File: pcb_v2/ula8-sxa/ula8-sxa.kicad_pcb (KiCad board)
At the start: 2 copper layers, 54.4 x 61 mm, 7 parts, among them J1 ula8a, U1 74LS244

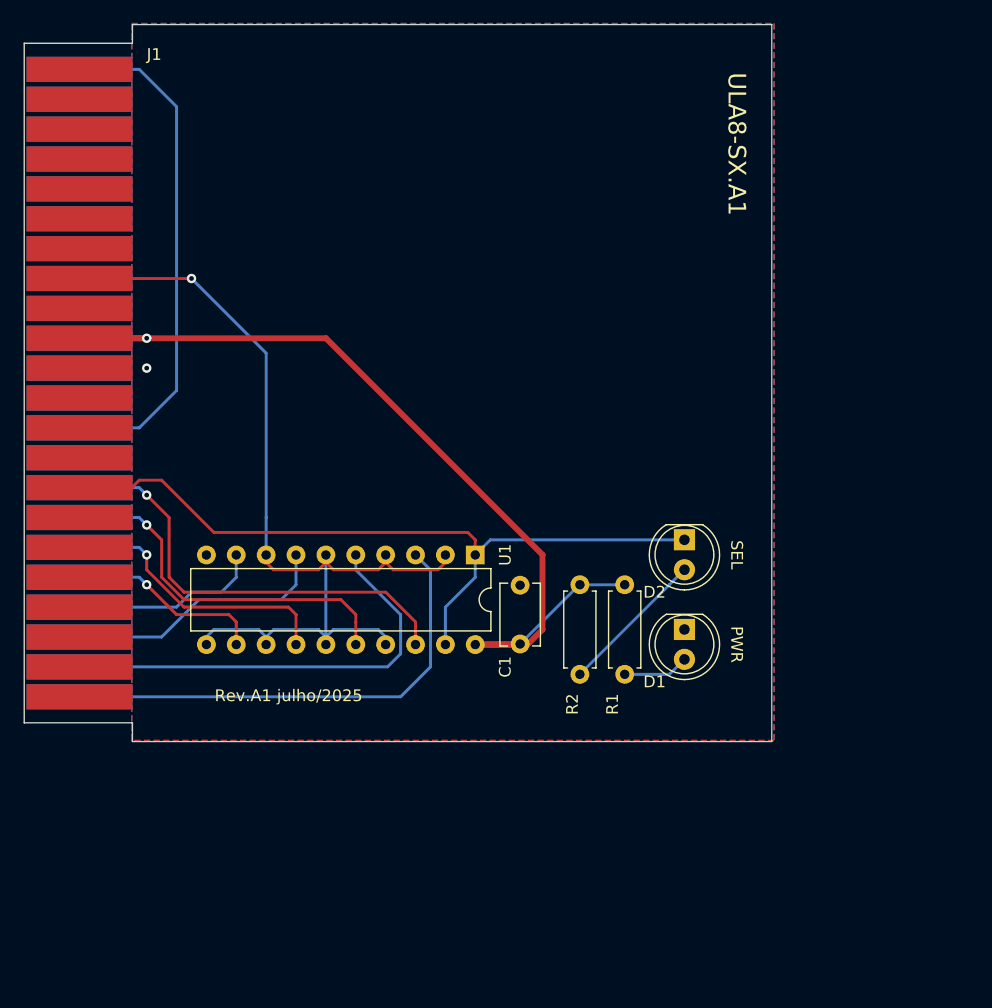
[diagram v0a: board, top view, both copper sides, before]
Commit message: deslocando alimentação para as estremidades do conector; carry out em três estados (ativo apenas quando select)
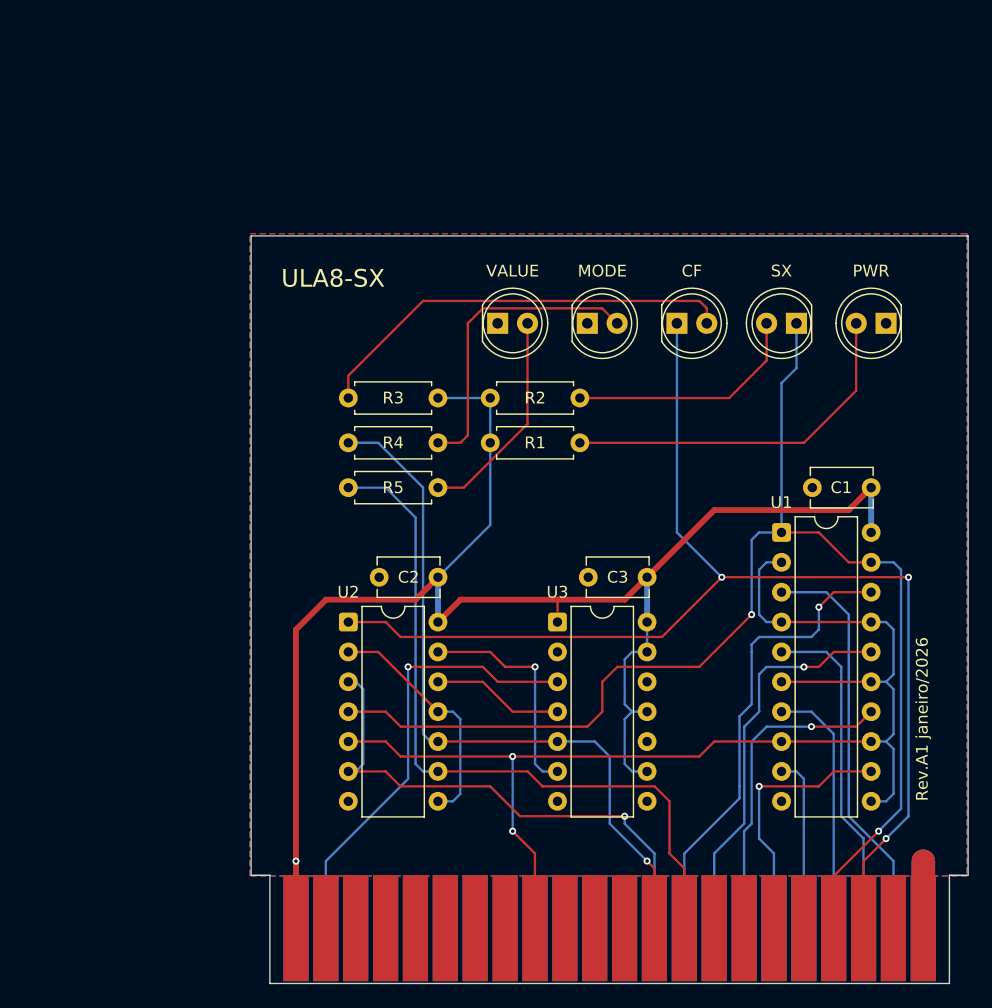
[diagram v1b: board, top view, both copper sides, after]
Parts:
- added C2: 100nF, Capacitor_THT:C_Disc_D5.1mm_W3.2mm_P5.00mm, F.Cu at (42.0, 57.1)
- added C3: 100nF, Capacitor_THT:C_Disc_D5.1mm_W3.2mm_P5.00mm, F.Cu at (59.8, 57.1)
- added D3: LED, LED_THT:LED_D5.0mm, F.Cu at (67.3, 35.6)
- added D4: LED, LED_THT:LED_D5.0mm, F.Cu at (59.7, 35.6)
- added D5: LED, LED_THT:LED_D5.0mm, F.Cu at (52.1, 35.6)
- added R3: 1K, Resistor_THT:R_Axial_DIN0207_L6.3mm_D2.5mm_P7.62mm_Horizontal, F.Cu at (47.0, 41.9)
- added R4: 1K, Resistor_THT:R_Axial_DIN0207_L6.3mm_D2.5mm_P7.62mm_Horizontal, F.Cu at (39.4, 45.7)
- added R5: 1K, Resistor_THT:R_Axial_DIN0207_L6.3mm_D2.5mm_P7.62mm_Horizontal, F.Cu at (39.4, 49.5)
- added U2: 74LS125, Package_DIP:DIP-14_W7.62mm, F.Cu at (39.4, 61.0)
- added U3: 74LS04, Package_DIP:DIP-14_W7.62mm, F.Cu at (57.1, 61.0)
- moved J1 75.3 mm to (34.9, 87.0), turned to 90 degrees
- moved D1 31.2 mm to (85.1, 35.6), turned to 180 degrees
- moved C1 26.2 mm to (78.8, 49.5), turned to 0 degrees
- moved U1 26.1 mm to (76.2, 53.3), turned to 0 degrees
- moved D2 20.7 mm to (77.5, 35.6), turned to 180 degrees
- moved R2 17.6 mm to (51.4, 41.9), turned to 0 degrees
- moved R1 16.6 mm to (51.4, 45.7), turned to 0 degrees
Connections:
- D2 pad 1: n_select -> ~{select_sx}
- J1 pad 1: unconnected-(J1-Pad1) -> +5V
- J1 pad 10: +5V -> unconnected-(J1-Pin_10-Pad10)
- J1 pad 11: GND -> unconnected-(J1-Pin_11-Pad11)
- J1 pad 13: unconnected-(J1-Pad13) -> option_mode
- J1 pad 14: unconnected-(J1-Pad14) -> option_value
- J1 pad 15: n_select -> unconnected-(J1-Pin_15-Pad15)
- J1 pad 19: unconnected-(J1-Pad19) -> ~{select_sx}
- J1 pad 20: unconnected-(J1-Pad20) -> ~{select_cf}
- J1 pad 22: unconnected-(J1-Pad22) -> GND
- J1 pad 23: /carry -> +5V
- J1 pad 24: unconnected-(J1-Pad24) -> carry_in
- J1 pad 32: +5V -> unconnected-(J1-Pin_32-Pad32)
- J1 pad 33: GND -> unconnected-(J1-Pin_33-Pad33)
- J1 pad 35: /carry -> carry_out
- J1 pad 36: unconnected-(J1-Pad36) -> ula_bus0
- J1 pad 37: ula_bus0 -> ula_bus1
- J1 pad 38: ula_bus1 -> ula_bus2
- J1 pad 39: ula_bus2 -> ula_bus3
- J1 pad 40: ula_bus3 -> ula_bus4
- J1 pad 41: ula_bus4 -> ula_bus5
- J1 pad 42: ula_bus5 -> ula_bus6
- J1 pad 43: ula_bus6 -> ula_bus7
- J1 pad 44: ula_bus7 -> GND
- J1 pad 8: lower_bus7 -> unconnected-(J1-Pin_8-Pad8)
- J1 pad 9: unconnected-(J1-Pad9) -> lower_bus7
- U1 pad 1: n_select -> ~{select_sx}
- U1 pad 19: n_select -> ~{select_sx}
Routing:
- net ~{select_sx}: track 0.00 -> 112.0 mm, vias 0 -> 2
- net ~{select_cf}: track 0.00 -> 104.8 mm, vias 0 -> 3
- net n_select: track 64.3 -> 0.00 mm
- net option_value: track 0.00 -> 61.9 mm
- net option_mode: track 0.00 -> 61.7 mm, vias 0 -> 1
- net +5V: track 80.1 -> 139.0 mm
- net carry_out: track 0.00 -> 45.1 mm, vias 0 -> 1
- net /carry: track 43.3 -> 0.00 mm
- net carry_in: track 0.00 -> 38.1 mm, vias 0 -> 1
- net Net-(D3-A): track 0.00 -> 36.5 mm
- net Net-(D4-A): track 0.00 -> 26.1 mm
- net Net-(D1-A): track 5.61 -> 31.1 mm
- net lower_bus7: track 84.5 -> 106.2 mm, vias 1 -> 2
- net Net-(U2-Pad11): track 0.00 -> 20.4 mm
- net Net-(U2-Pad13): track 0.00 -> 19.2 mm, vias 0 -> 1
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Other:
- board size 54.4 x 61 mm -> 61 x 54.4 mm
- board text added: "CF"
- board text added: "MODE"
- board text added: "Rev.A1 janeiro/2026"
- board text added: "SX"
- board text added: "ULA8-SX"
- board text added: "VALUE"
- board text removed: "Rev.A1 julho/2025"
- board text removed: "SEL"
- board text removed: "ULA8-SX.A1"
